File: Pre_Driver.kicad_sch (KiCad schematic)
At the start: 1 part

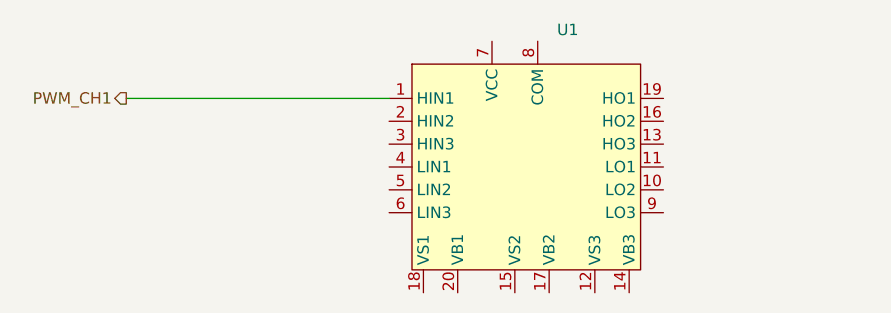
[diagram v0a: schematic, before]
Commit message: 增加部分接口
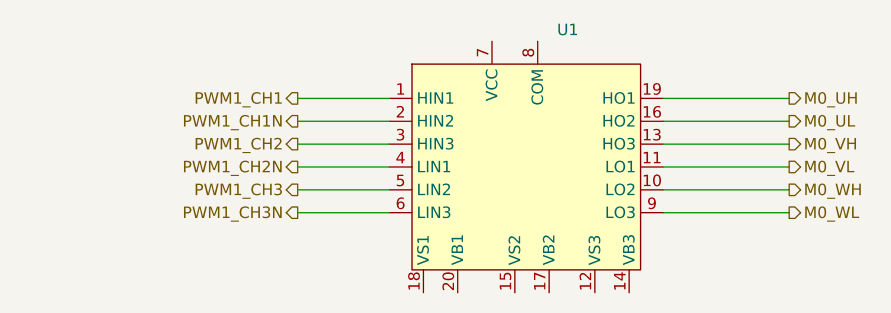
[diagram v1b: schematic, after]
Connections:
- net M0_WH: now reaches U1.10 (LO2)
- net M0_VL: now reaches U1.11 (LO1)
- net M0_VH: now reaches U1.13 (HO3)
- net M0_UL: now reaches U1.16 (HO2)
- net M0_UH: now reaches U1.19 (HO1)
- net PWM1_CH1N: now reaches U1.2 (HIN2)
- net PWM1_CH2: now reaches U1.3 (HIN3)
- net PWM1_CH2N: now reaches U1.4 (LIN1)
- net PWM1_CH3: now reaches U1.5 (LIN2)
- net PWM1_CH3N: now reaches U1.6 (LIN3)
- net M0_WL: now reaches U1.9 (LO3)
- net PWM_CH1 renamed PWM1_CH1
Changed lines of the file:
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@@
 	(wire
 		(pts
-			(xy 64.77 72.39) (xy 93.98 72.39)
-		)
-		(stroke
-			(width 0)
-			(type default)
-		)
-	)
-	(hierarchical_label "PWM_CH1"
-		(shape output)
-		(at 64.77 72.39 180)
-		(effects
-			(font
+			(xy 83.82 77.47) (xy 93.98 77.47)
+		)
+		(stroke
+			(width 0)
+			(type default)
+		)
+	)
+	(wire
+		(pts
+			(xy 124.46 74.93) (xy 138.43 74.93)
+		)
+		(stroke
+			(width 0)
+			(type default)
+		)
+	)
+	(wire
+		(pts
+			(xy 83.82 74.93) (xy 93.98 74.93)
+		)
+		(stroke
+			(width 0)
+			(type default)
+		)
+	)
+	(wire
+		(pts
+			(xy 124.46 82.55) (xy 138.43 82.55)
+		)
+		(stroke
+			(width 0)
+			(type default)
+		)
+	)
+	(wire
+		(pts
+			(xy 124.46 77.47) (xy 138.43 77.47)
+		)
+		(stroke
+			(width 0)
+			(type default)
+		)
+	)
+	(wire
+		(pts
+			(xy 124.46 85.09) (xy 138.43 85.09)
+		)
+		(stroke
+			(width 0)
+			(type default)
+		)
+	)
+	(wire
+		(pts
+			(xy 83.82 85.09) (xy 93.98 85.09)
+		)
+		(stroke
+			(width 0)
+			(type default)
+		)
+	)
+	(wire
+		(pts
+			(xy 124.46 72.39) (xy 138.43 72.39)
+		)
+		(stroke
+			(width 0)
+			(type default)
+		)
+	)
+	(wire
+		(pts
+			(xy 83.82 80.01) (xy 93.98 80.01)
+		)
+		(stroke
+			(width 0)
+			(type default)
+		)
+	)
+	(wire
+		(pts
+			(xy 83.82 82.55) (xy 93.98 82.55)
+		)
+		(stroke
+			(width 0)
+			(type default)
+		)
+	)
+	(wire
+		(pts
+			(xy 124.46 80.01) (xy 138.43 80.01)
+		)
+		(stroke
+			(width 0)
+			(type default)
+		)
+	)
+	(wire
+		(pts
+			(xy 83.82 72.39) (xy 93.98 72.39)
+		)
+		(stroke
+			(width 0)
+			(type default)
+		)
+	)
+	(hierarchical_label "M0_UL"
+		(shape output)
+		(at 138.43 74.93 0)
+		(effects
+			(font
+				(size 1.27 1.27)
+			)
+			(justify left)
+		)
+	)
+	(hierarchical_label "M0_UH"
+		(shape output)
+		(at 138.43 72.39 0)
+		(effects
+			(font
+				(size 1.27 1.27)
+			)
+			(justify left)
+		)
+	)
+	(hierarchical_label "M0_VL"
+		(shape output)
+		(at 138.43 80.01 0)
+		(effects
+			(font
+				(size 1.27 1.27)
+			)
+			(justify left)
+		)
+	)
+	(hierarchical_label "PWM1_CH3N"
+		(shape output)
+		(at 83.82 85.09 180)
+		(effects
+			(font
+				(size 1.27 1.27)
+			)
+			(justify right)
+		)
+	)
+	(hierarchical_label "PWM1_CH1N"
+		(shape output)
+		(at 83.82 74.93 180)
+		(effects
+			(font
+				(size 1.27 1.27)
+			)
+			(justify right)
+		)
+	)
+	(hierarchical_label "PWM1_CH2"
+		(shape output)
+		(at 83.82 77.47 180)
+		(effects
+			(font
+				(size 1.27 1.27)
+			)
+			(justify right)
+		)
+	)
+	(hierarchical_label "M0_WH"
+		(shape output)
+		(at 138.43 82.55 0)
+		(effects
+			(font
+				(size 1.27 1.27)
+			)
+			(justify left)
+		)
+	)
+	(hierarchical_label "M0_VH"
+		(shape output)
+		(at 138.43 77.47 0)
+		(effects
+			(font
+				(size 1.27 1.27)
+			)
+			(justify left)
+		)
+	)
+	(hierarchical_label "PWM1_CH2N"
+		(shape output)
+		(at 83.82 80.01 180)
+		(effects
+			(font
+				(size 1.27 1.27)
+			)
+			(justify right)
+		)
+	)
+	(hierarchical_label "PWM1_CH1"
+		(shape output)
+		(at 83.82 72.39 180)
+		(effects
+			(font
+				(size 1.27 1.27)
+			)
+			(justify right)
+		)
+	)
+	(hierarchical_label "M0_WL"
+		(shape output)
+		(at 138.43 85.09 0)
+		(effects
+			(font
+				(size 1.27 1.27)
+			)
+			(justify left)
+		)
+	)
+	(hierarchical_label "PWM1_CH3"
+		(shape output)
+		(at 83.82 82.55 180)
+		(effects
+			(font

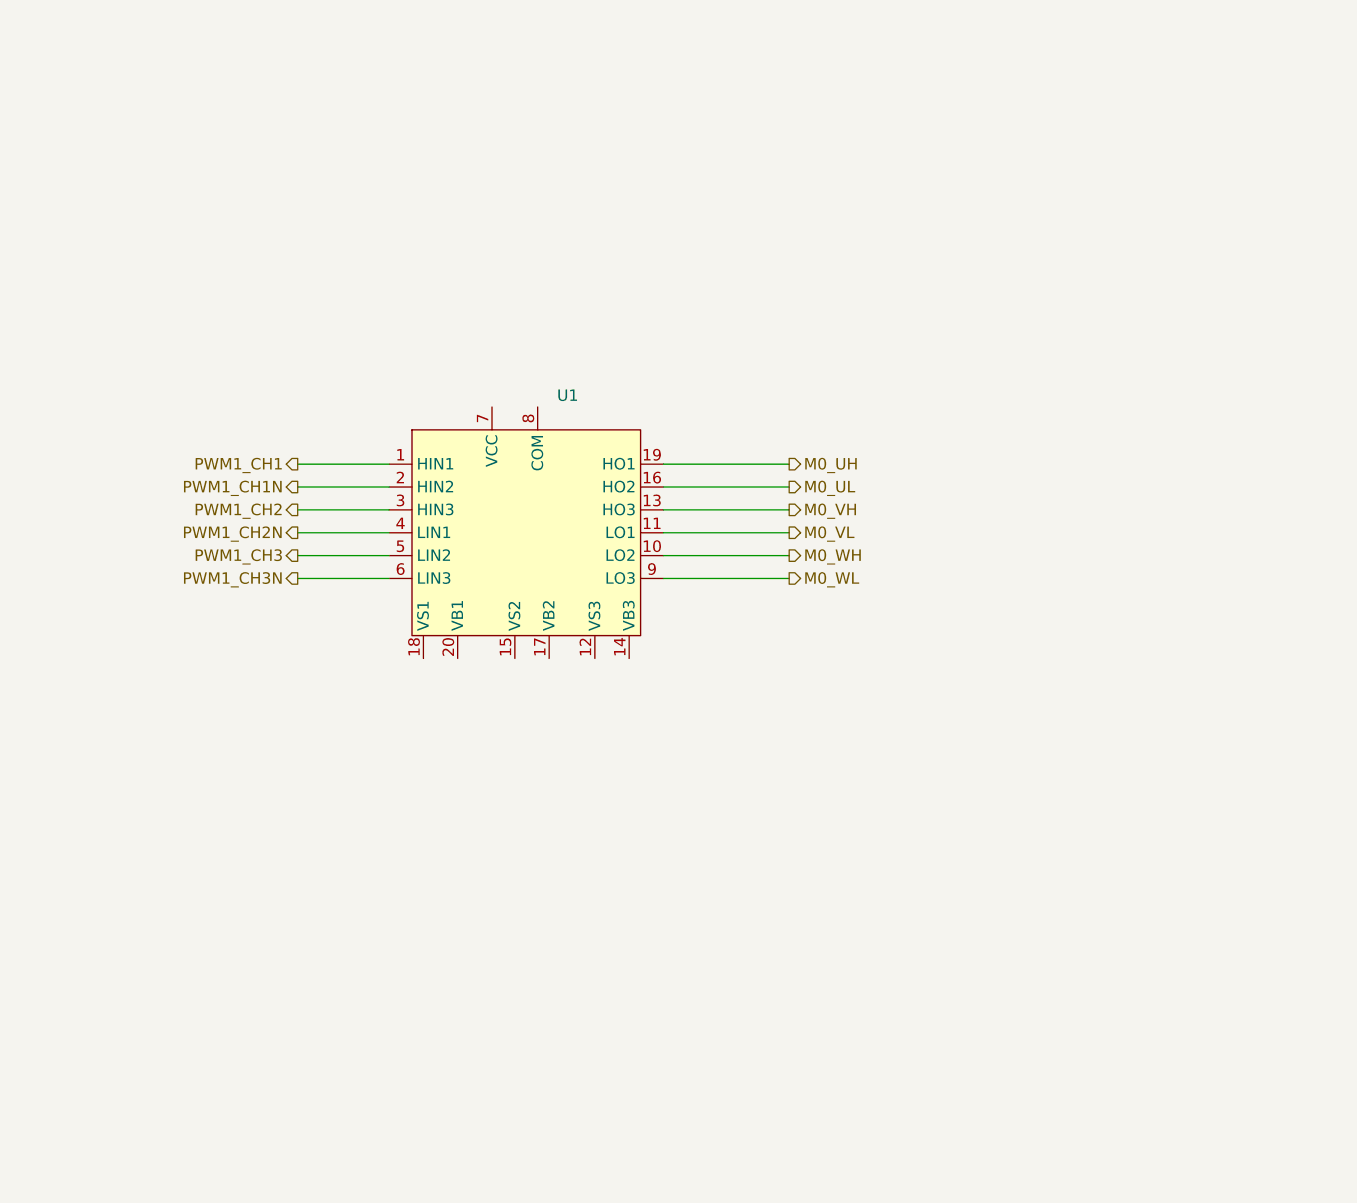
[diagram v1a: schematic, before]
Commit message: 优化5V电源/预驱电路/三相桥/运放
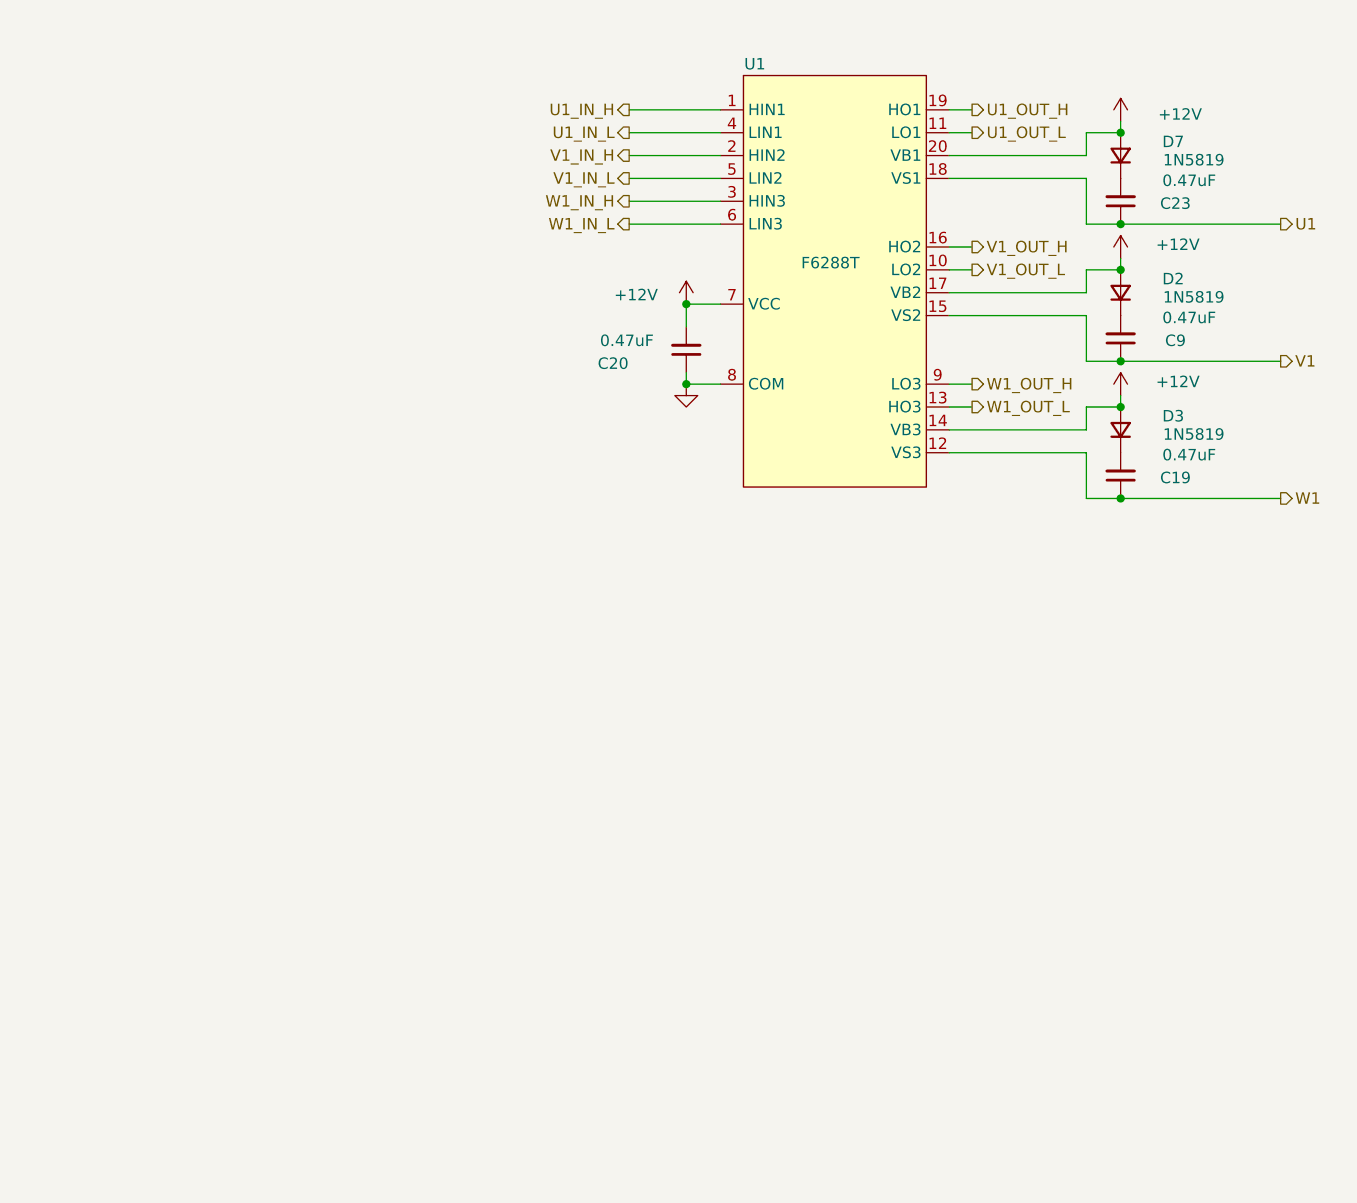
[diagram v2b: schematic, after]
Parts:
- removed U1: ~, symbol User_Driver:FD6288T
- added C19, C20, C23, C9: 0.47uF, Capacitor_SMD:C_0805_2012Metric, symbol Device:C_Small
- added D2, D3, D7: 1N5819, Diode_SMD:D_SOD-123, symbol Device:D_Small
- added U1: F6288T, symbol User_Driver:FD6288
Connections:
- new net: C9.2, D2.1 (K)
- new net: C19.2, D3.1 (K)
- new net: C23.2, D7.1 (K)
- new net +12V: C20.2, D2.2 (A), D3.2 (A), D7.2 (A), U1.14 (VB3), U1.17 (VB2), U1.20 (VB1), U1.7 (VCC)
- new net GND: C20.1, U1.8 (COM)
- new net U1: C23.1, U1.18 (VS1)
- new net U1_IN_H: U1.1 (HIN1)
- new net U1_IN_L: U1.4 (LIN1)
- new net U1_OUT_H: U1.19 (HO1)
- new net U1_OUT_L: U1.11 (LO1)
- new net V1: C9.1, U1.15 (VS2)
- new net V1_IN_H: U1.2 (HIN2)
- new net V1_IN_L: U1.5 (LIN2)
- new net V1_OUT_H: U1.16 (HO2)
- new net V1_OUT_L: U1.10 (LO2)
- new net W1: C19.1, U1.12 (VS3)
- new net W1_IN_H: U1.3 (HIN3)
- new net W1_IN_L: U1.6 (LIN3)
- new net W1_OUT_H: U1.9 (LO3)
- new net W1_OUT_L: U1.13 (HO3)

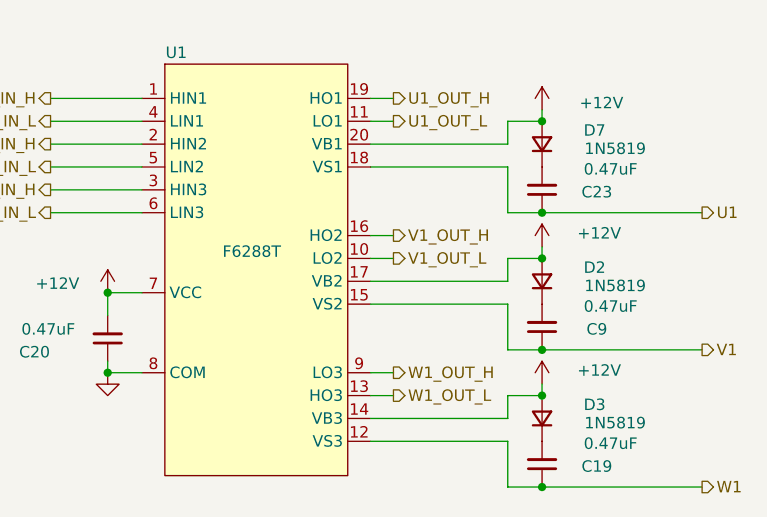
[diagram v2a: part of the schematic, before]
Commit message: 分配部分封装
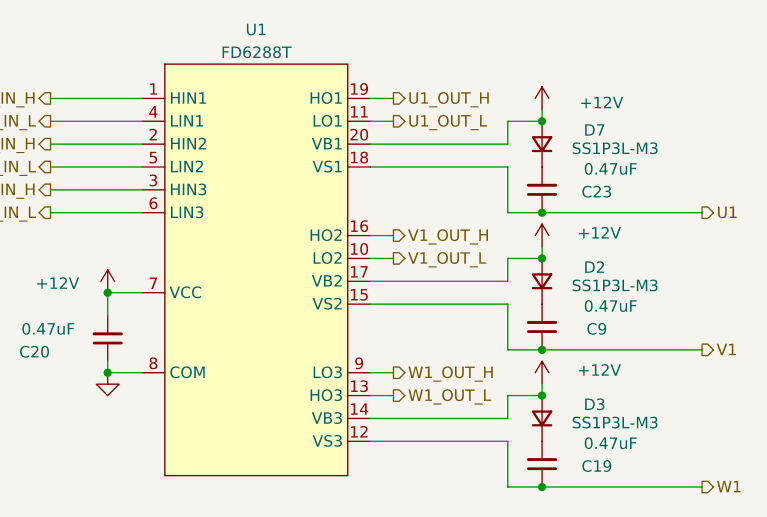
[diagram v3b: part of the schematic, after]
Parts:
- D2, D3, D7: value 1N5819 -> SS1P3L-M3; footprint Diode_SMD:D_SOD-123 -> Diode_SMD:D_SMP_DO-220AA
- U1: value F6288T -> FD6288T; footprint (none) -> Package_SO:TSSOP-20_4.4x6.5mm_P0.65mm

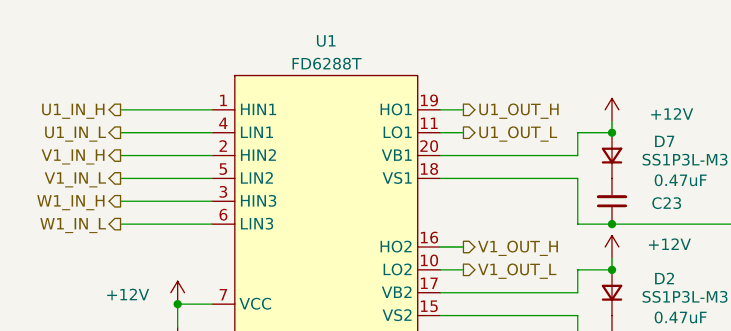
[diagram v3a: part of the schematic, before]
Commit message: 生成网表并添加到PCB
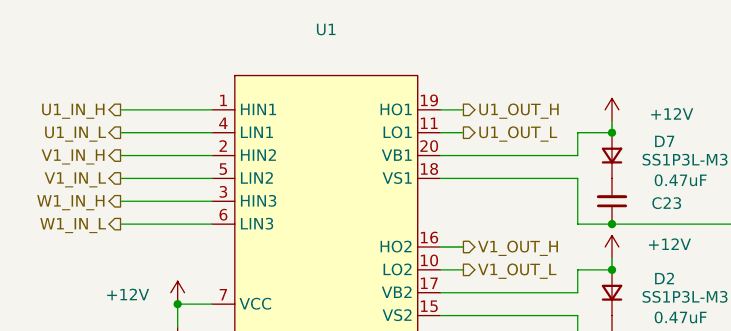
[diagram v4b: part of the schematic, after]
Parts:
- U1: value FD6288T -> ~; footprint Package_SO:TSSOP-20_4.4x6.5mm_P0.65mm -> Package_SO:TSSOP-20_4.4x5mm_P0.5mm
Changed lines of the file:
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@@
+	)
+	(symbol
+		(lib_id "User_Driver:FD6288")
+		(at 133.35 29.21 0)
+		(unit 1)
+		(exclude_from_sim no)
+		(in_bom yes)
+		(on_board yes)
+		(dnp no)
+		(fields_autoplaced yes)
+		(property "Reference" "U1"
+			(at 143.51 24.13 0)
+			(effects
+				(font
+					(size 1.27 1.27)
+				)
+			)
+		)
+		(property "Value" "~"
+			(at 143.51 26.67 0)
+			(effects
+				(font
+					(size 1.27 1.27)
+				)
+			)
+		)
+		(property "Footprint" "Package_SO:TSSOP-20_4.4x5mm_P0.5mm"
+			(at 133.35 29.21 0)
+			(effects
+				(font
+					(size 1.27 1.27)
+				)
+				(hide yes)
+			)
+		)
+		(property "Datasheet" ""
+			(at 133.35 29.21 0)
+			(effects
+				(font
+					(size 1.27 1.27)
+				)
+				(hide yes)
+			)
+		)
+		(property "Description" ""
+			(at 133.35 29.21 0)
+			(effects
+				(font
+					(size 1.27 1.27)
+				)
+				(hide yes)
+			)
+		)
+		(pin "15"
+		)
+		(pin "13"
+		)
+		(pin "17"
+		)
+		(pin "7"
+		)
+		(pin "6"
+		)
+		(pin "3"
+		)
+		(pin "16"
+		)
+		(pin "8"
+		)
+		(pin "12"
+		)
+		(pin "18"
+		)
+		(pin "11"
+		)
+		(pin "20"
+		)
+		(pin "10"
+		)
+		(pin "19"
+		)
+		(pin "9"
+		)
+		(pin "14"
+		)
+		(pin "5"
+		)
+		(pin "2"
+		)
+		(pin "4"
+		)
+		(pin "1"
+		)
+		(instances
+			(project ""
+				(path "/6b2aea6d-5084-4a15-abee-69a455b7078c/bd1ee54e-e470-4e6c-b487-ecc2bf967c4b"
+					(reference "U1")
+					(unit 1)
+				)
+			)
+		)
 	)
 	(symbol
@@
 					(unit 1)
 				)
-			)
-		)
-	)
-	(symbol
-		(lib_id "User_Driver:FD6288")
-		(at 133.35 29.21 0)
-		(unit 1)
-		(exclude_from_sim no)
-		(in_bom yes)
-		(on_board yes)
-		(dnp no)
-		(fields_autoplaced yes)
-		(property "Reference" "U1"
-			(at 143.51 25.4 0)
-			(effects
-				(font
-					(size 1.27 1.27)
-				)
-			)
-		)
-		(property "Value" "FD6288T"
-			(at 143.51 27.94 0)
-			(effects
-				(font
-					(size 1.27 1.27)
-				)
-			)
-		)
-		(property "Footprint" "Package_SO:TSSOP-20_4.4x6.5mm_P0.65mm"
-			(at 133.35 29.21 0)
-			(effects
-				(font
-					(size 1.27 1.27)
-				)
-				(hide yes)
-			)
-		)
-		(property "Datasheet" ""
-			(at 133.35 29.21 0)
-			(effects
-				(font
-					(size 1.27 1.27)
-				)
-				(hide yes)
-			)
-		)
-		(property "Description" ""
-			(at 133.35 29.21 0)
-			(effects
-				(font
-					(size 1.27 1.27)
-				)
-				(hide yes)
-			)
-		)
-		(pin "20"
-		)
-		(pin "19"
-		)
-		(pin "6"
-		)
-		(pin "11"
-		)
-		(pin "5"
-		)
-		(pin "3"
-		)
-		(pin "14"
-		)
-		(pin "12"
-		)
-		(pin "9"
-		)
-		(pin "13"
-		)
-		(pin "2"
-		)
-		(pin "4"
-		)
-		(pin "18"
-		)
-		(pin "16"
-		)
-		(pin "1"
-		)
-		(pin "7"
-		)
-		(pin "15"
-		)
-		(pin "17"
-		)
-		(pin "10"
-		)
-		(pin "8"
-		)
-		(instances
-			(project ""
-				(path "/6b2aea6d-5084-4a15-abee-69a455b7078c/bd1ee54e-e470-4e6c-b487-ecc2bf967c4b"
-					(reference "U1")
-					(unit 1)
-				)
